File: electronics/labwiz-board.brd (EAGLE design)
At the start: 98.8 x 51 mm, 100 parts, among them J1 SD_MICRO_SDIO_1BIT, J2 CORTEX_DEBUGSMD_original, J3 DNP, U1 STM32F10XRXT6, U2 MCP73831/2, U4 MIC5219-3.3V, X2 M12_BOTTOM_CONTACTS_FPC_1MM, Y3 32.768kHz

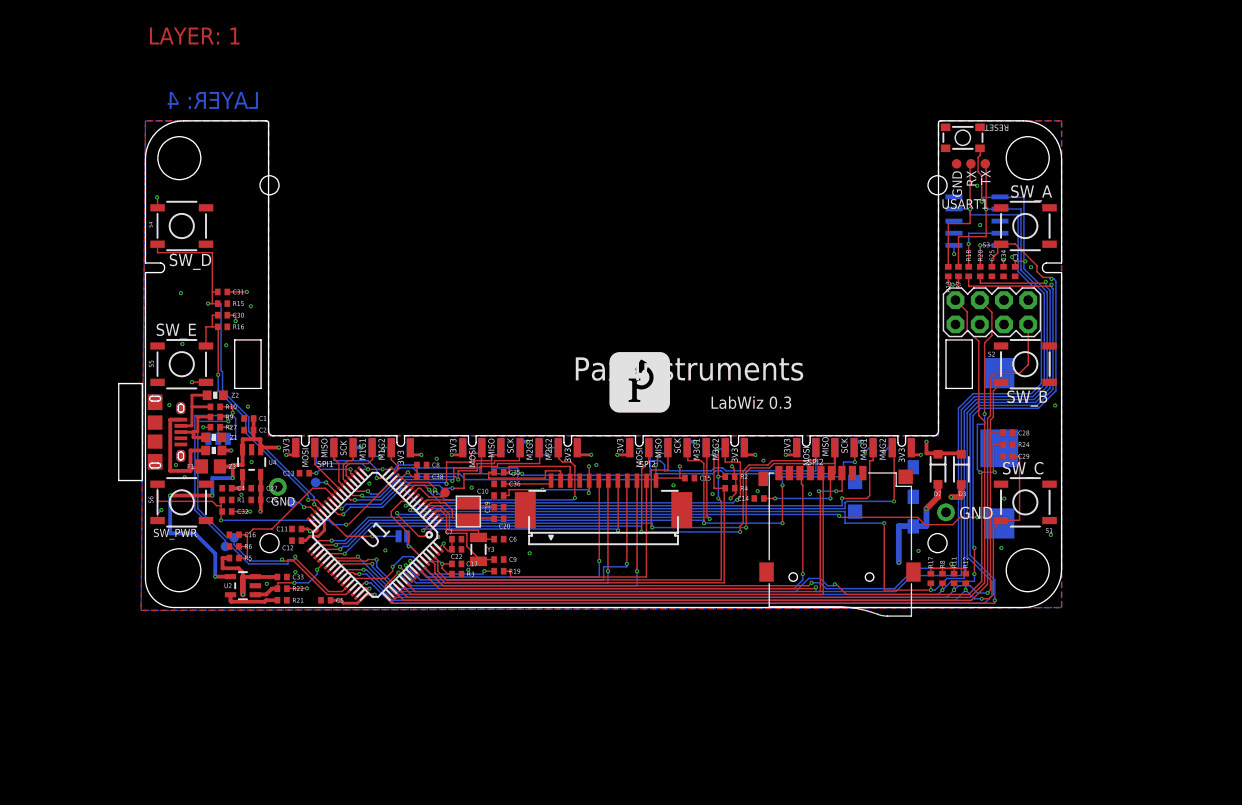
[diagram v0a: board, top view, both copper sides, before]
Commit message: Changed board top edge; extended 24 mil, created protrusion to lock in with top panel of enclosure. Closes #97.
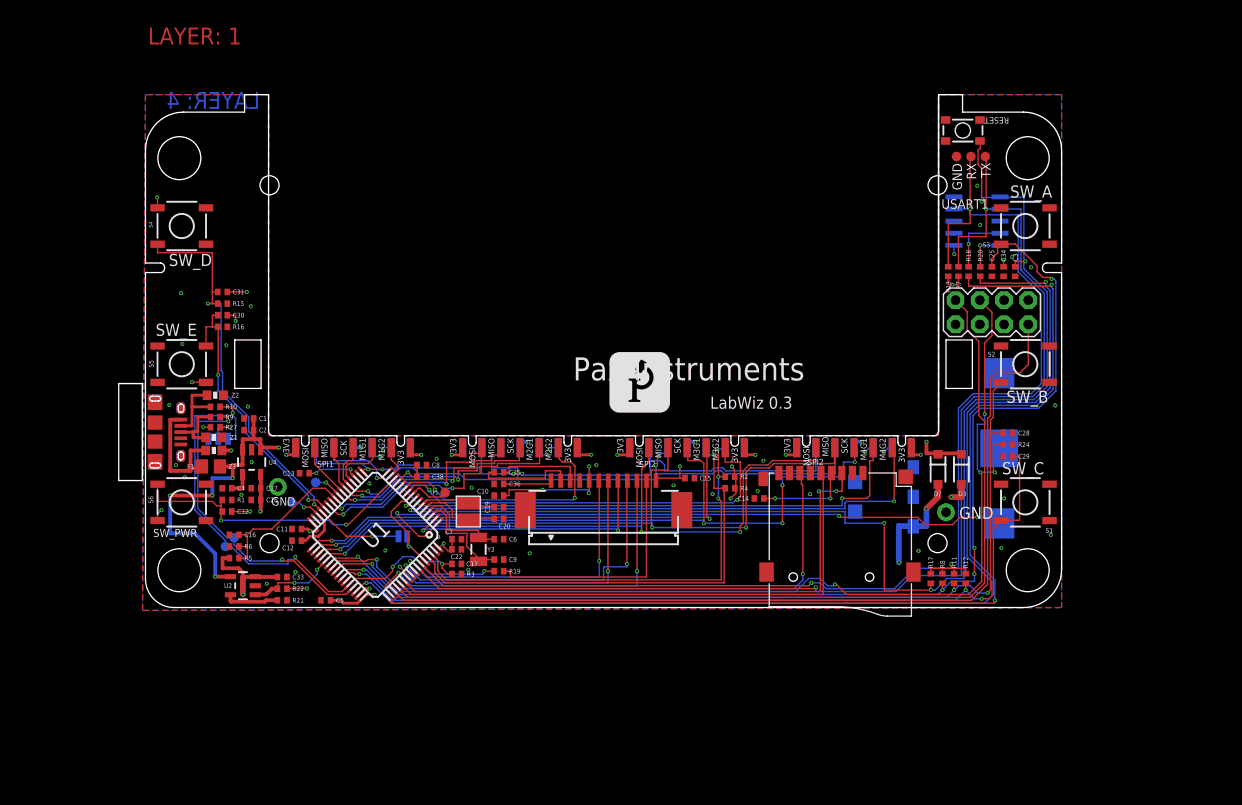
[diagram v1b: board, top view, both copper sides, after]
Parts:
- moved S7 0.76 mm to (85.6, 50.0)
- moved TP10 0.76 mm to (85.0, 47.3)
- moved TP8 0.76 mm to (88.0, 47.3)
- moved TP9 0.76 mm to (86.5, 47.3)
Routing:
- net USART1_TX: track 122.9 -> 123.7 mm
- net USART1_RX: track 124.6 -> 125.4 mm
- net NRST: track 129.7 -> 130.4 mm
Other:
- board size 98.8 x 51 mm -> 98.8 x 53.7 mm

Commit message: Added 2x2 right angle header to board. Closes #105.
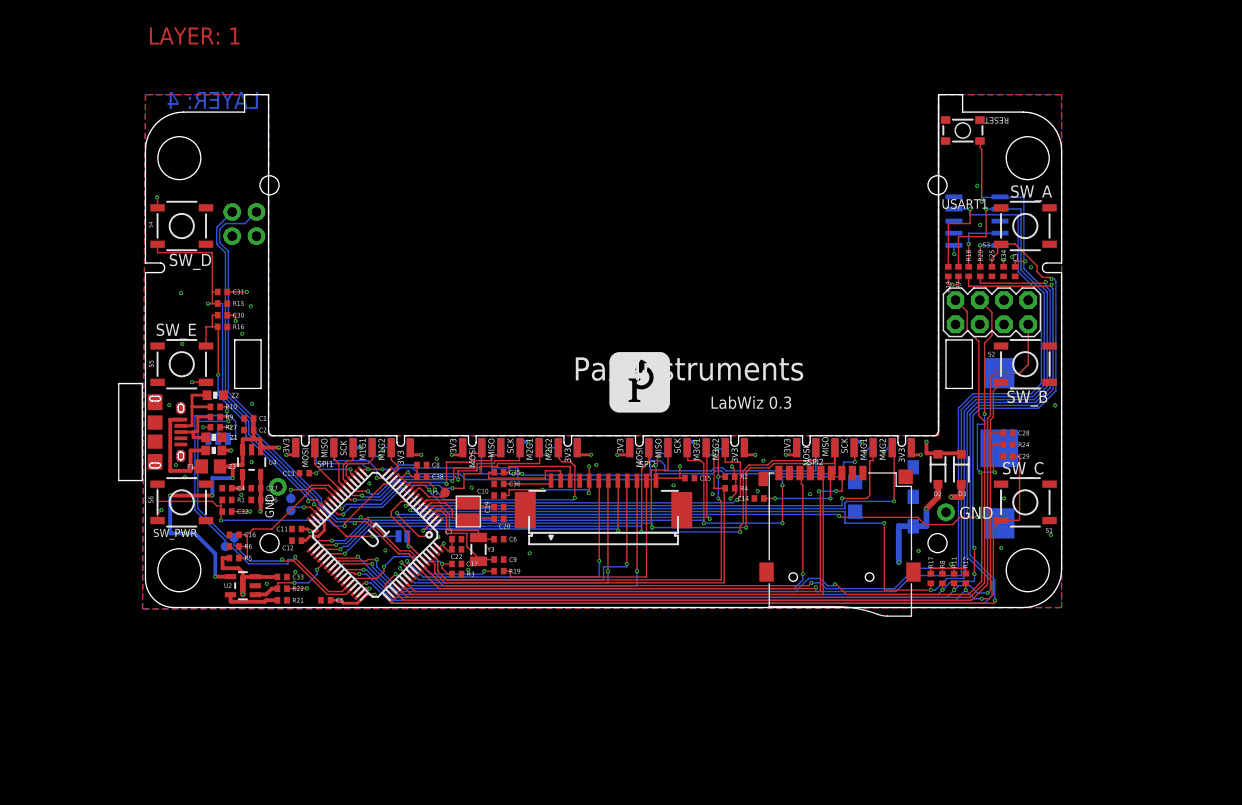
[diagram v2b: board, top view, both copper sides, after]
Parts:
- removed TP10, TP8, TP9: DNP, PaxInstruments-Connectors:PAD_1MM
- added U$5: USART1, PaxInstruments-Connectors:M02X2_TH_RIGHT_ANGLE
- moved TP2 3.09 mm to (15.2, 11.4)
- moved TP7 0.86 mm to (15.2, 10.2)
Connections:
- net GND: now also U$5.4; no longer TP10.P$1
- net USART1_RX: now also U$5.3; no longer TP9.P$1
- net USART1_TX: now also U$5.1; no longer TP8.P$1
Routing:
- net USART1_RX: track 125.4 -> 171.0 mm, vias 2 -> 3
- net USART1_TX: track 123.7 -> 167.6 mm, vias 2 -> 3
- net PC4: track 2.92 -> 6.48 mm
- net LCD_RST: track 35.5 -> 36.6 mm
- net USB_DM: track 40.9 -> 40.1 mm

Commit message: Moved to ESP-09 WiFi modules. Still some work to be done.
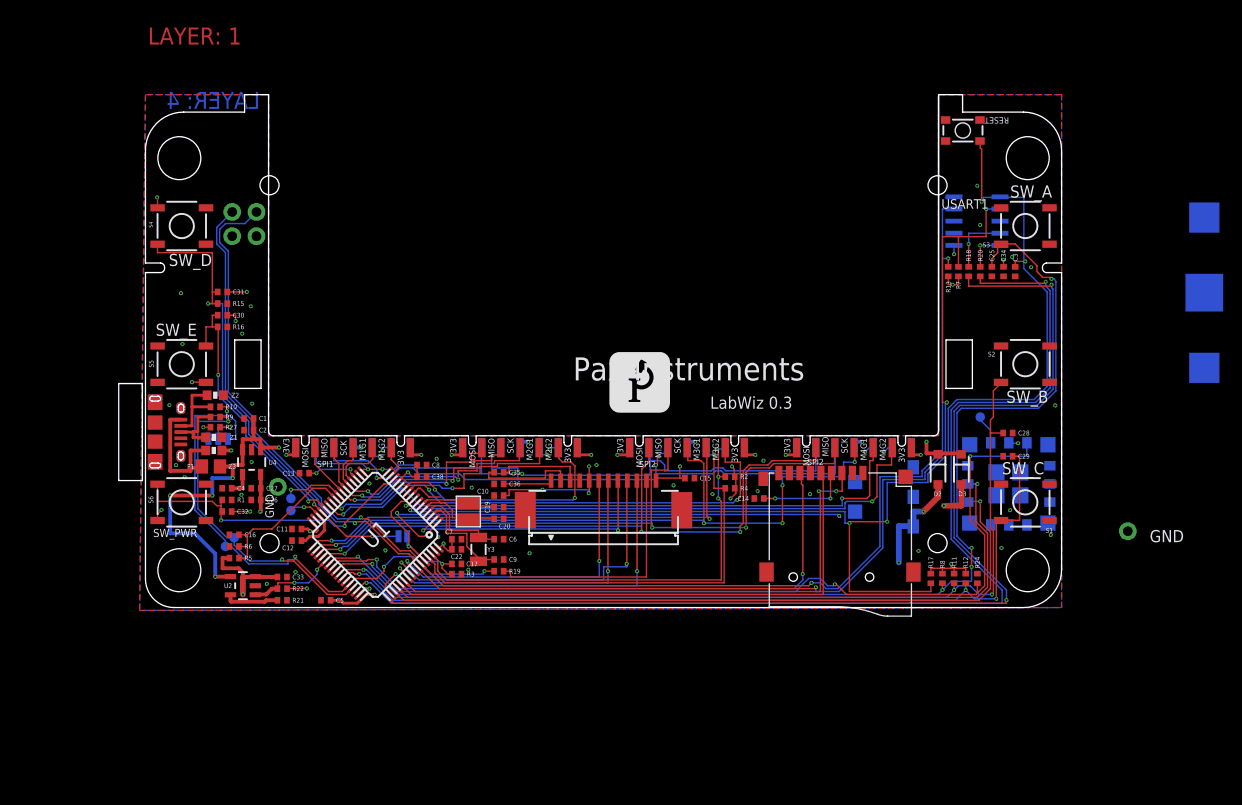
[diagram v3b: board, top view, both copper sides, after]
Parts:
- removed J3: DNP, SparkFun-Connectors:2X4
- added U$7: ESP09, PaxInstruments-DigitalIC:ESP09
- moved TP1 56.6 mm to (87.5, 20.0), flipped to the bottom
- moved BAT1 27.0 mm to (111.0, 33.0)
- moved TP3 19.2 mm to (102.9, 8.00)
- moved R24 14.4 mm to (87.2, 3.05), turned to 90 degrees
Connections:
- new net N$13: TP1.P$1, U$7.ANT
- net 3.3V: now also U$7.VCC; no longer J3.8
- net GND: now also U$7.GND, U$7.GND1, U$7.GND2, U$7.GND3, U$7.GND4, U$7.GND5, U$7.GND6, U$7.GND7; no longer J3.1
- net PC1_BOOT0: no longer TP1.P$1
- net USART3_RX: now also U$7.TX; no longer J3.2
- net USART3_TX: now also U$7.RX; no longer J3.7
- net WIFI_EN: now also U$7.CH_PD; no longer J3.4
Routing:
- net USART1_RX: track 171.0 -> 145.6 mm
- net USART3_TX: track 93.6 -> 74.2 mm, vias 0 -> 1
- net USART3_RX: track 93.3 -> 75.0 mm, vias 0 -> 1
- net RTC_BAT: track 70.7 -> 52.8 mm, vias 3 -> 2
- net USART1_TX: track 167.6 -> 151.9 mm, vias 3 -> 4
- net WIFI_EN: track 108.4 -> 95.2 mm, vias 5 -> 3
- net SWDIO: track 117.3 -> 121.8 mm
- net SWCLK: track 115.2 -> 119.5 mm
- net N$13: track 0.00 -> 3.16 mm
- net 3.3V: track 97.2 -> 99.8 mm, vias 36 -> 37
- net SW_A: track 120.8 -> 123.1 mm
- net NRST: track 130.2 -> 131.6 mm
- net SW_B: track 95.2 -> 95.9 mm
- net MOD4_GPIO2: track 59.1 -> 58.4 mm
- net PC1_BOOT0: track 22.2 -> 21.6 mm

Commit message: Added pin interrupt info to a page on the pin-map spreadsheet. Changed RTC battery to a CR1025. CR1025 connections still need to be routed.
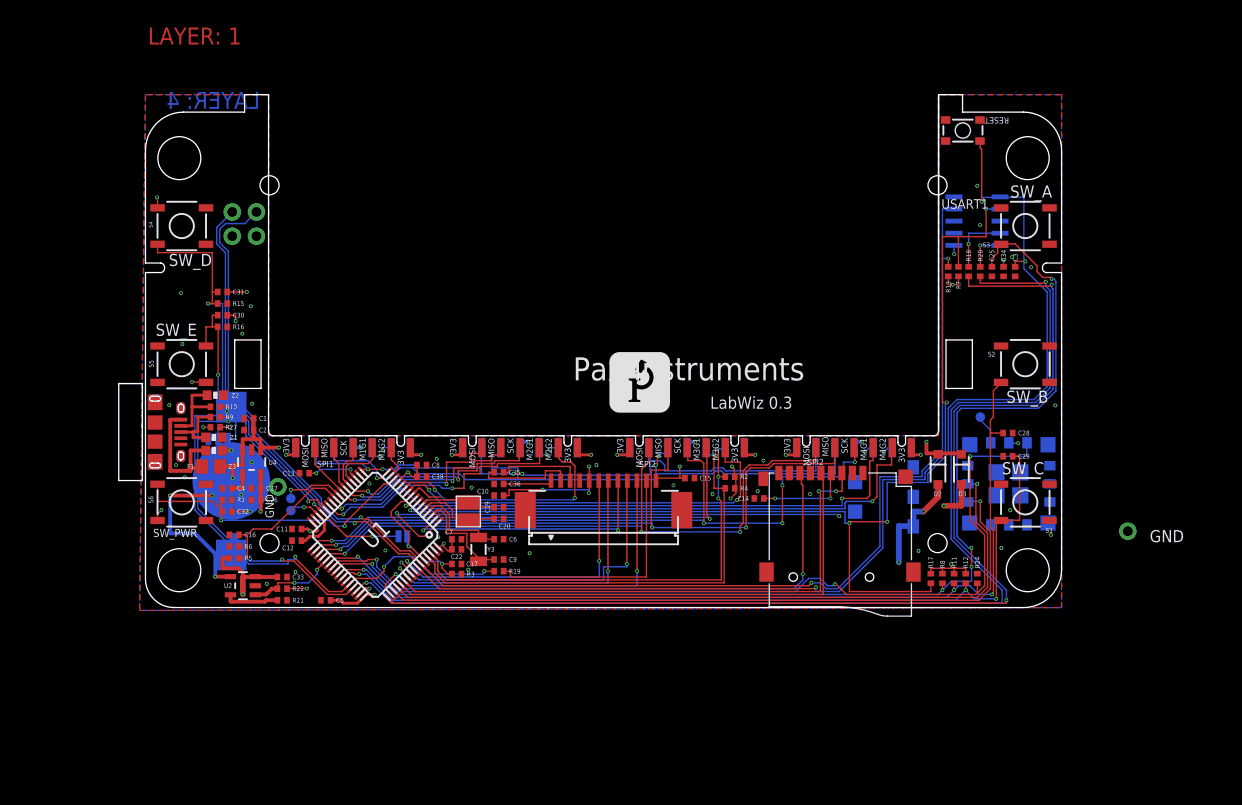
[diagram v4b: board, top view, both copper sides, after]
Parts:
- removed BAT1: (no value), PaxInstruments-Electromechanical:BATTCON_12MM
- added U$8: CR1025, PaxInstruments-Electromechanical:CR2025
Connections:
- net GND: now also U$8.P$1; no longer BAT1.GND
- net RTC_BAT: now also U$8.P$2, U$8.P$3; no longer BAT1.PWR@1
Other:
- board text added: "10 mm CR1025"
- board text added: "12.5 mm CR1220 in T400"

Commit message: Routed the RTC battery. Bumped a bunch of traces around.
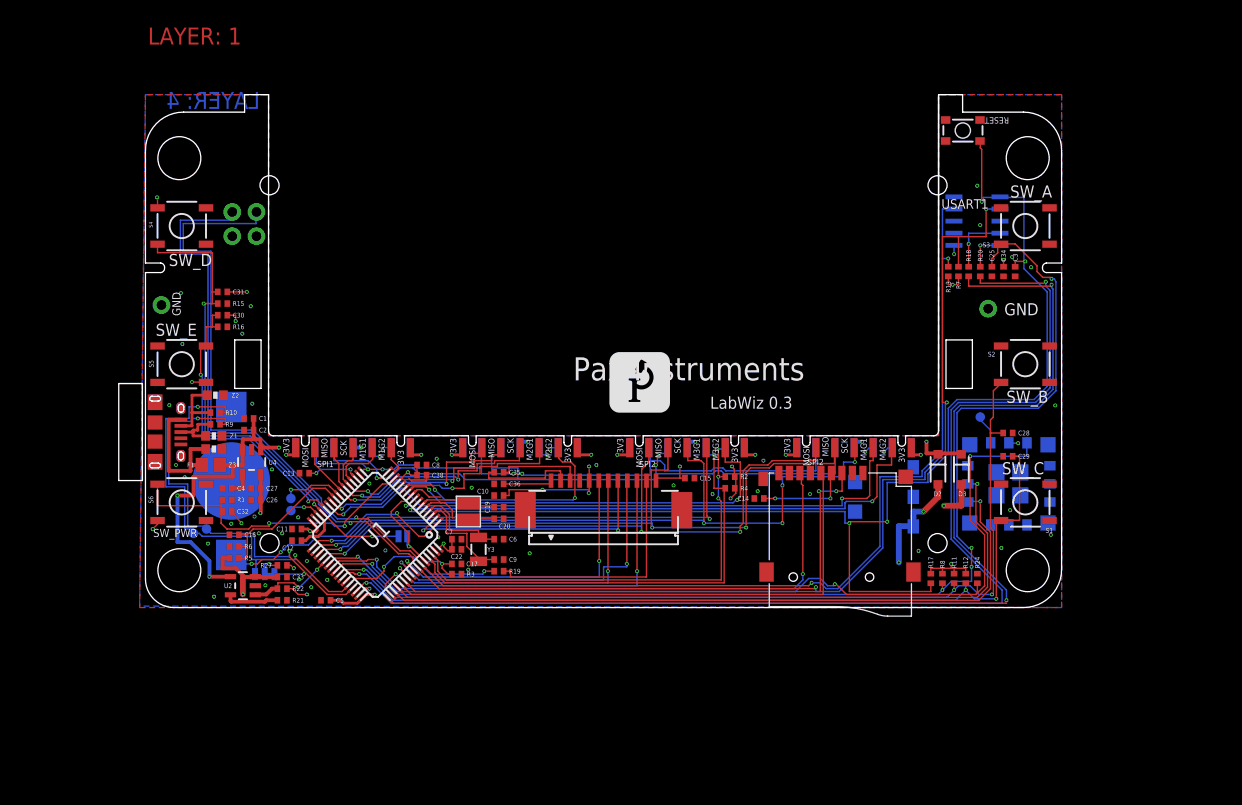
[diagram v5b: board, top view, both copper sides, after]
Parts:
- moved TP3 27.5 mm to (88.3, 31.3)
- moved TP4 22.6 mm to (1.68, 31.7)
- moved R27 16.1 mm to (14.3, 4.42), turned to 0 degrees
- moved JP2 15.0 mm to (12.5, 3.51), turned to 180 degrees
- moved TP6 3.62 mm to (5.03, 7.77)
- moved TP5 3.04 mm to (6.40, 8.23)
- moved R9 0.76 mm to (7.32, 19.2)
- moved R10 0.61 mm to (7.32, 20.4)
- moved C38 0.15 mm to (29.0, 13.9)
- moved F1 0.15 mm to (6.86, 14.9)
- moved Z1 0.15 mm to (7.16, 18.0)
- moved Z3 0.15 mm to (7.16, 16.6)
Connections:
- new net +: U$8.P$2
- net RTC_BAT: no longer U$8.P$2
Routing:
- net RTC_BAT: track 52.8 -> 26.3 mm, vias 2 -> 3
- net USB_DP: track 36.5 -> 48.0 mm, vias 2 -> 3
- net USART1_TX: track 151.9 -> 162.7 mm
- net USART1_RX: track 145.6 -> 156.4 mm
- net USB_DM: track 40.1 -> 46.6 mm
- net SW_D_BOOT0: track 50.3 -> 52.9 mm
- net SW_E_BOOT1: track 29.4 -> 31.6 mm
- net GND: track 2.40 -> 4.01 mm, vias 36 -> 44
- net VBUS: track 123.2 -> 121.8 mm, vias 10 -> 8
- net SW_PWR: track 31.7 -> 32.9 mm
- net N$5: track 3.46 -> 2.55 mm
- net D+: track 6.57 -> 5.65 mm
- net USB_VCC: track 13.7 -> 14.3 mm
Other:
- board text removed: "10 mm CR1025"
- board text removed: "12.5 mm CR1220 in T400"

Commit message: PC4 is now VBUS_DETECT. Removed unnecessary USB data series resistors. Closes #76.'
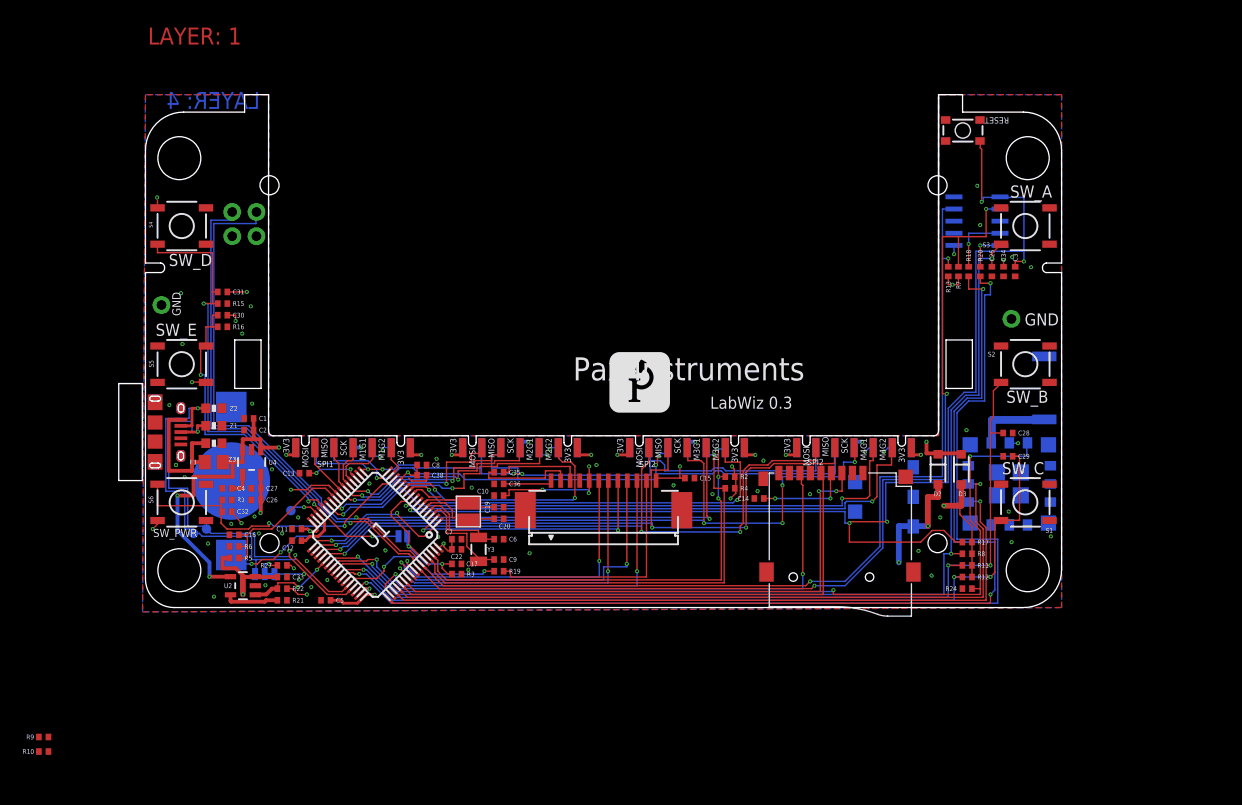
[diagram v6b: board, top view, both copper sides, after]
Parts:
- removed TP1, TP2: DNP, PaxInstruments-Connectors:PAD_1MM
- added U$10: 2.45GHz, SparkFun-RF:ANT-2.4GHZ-6.5X2.2MM
- R10: value 22R -> 47k
- R9: value 22R -> 68k
- moved R10 39.8 mm to (-10.7, -15.1)
- moved R9 37.4 mm to (-10.7, -13.6)
- moved R17 5.39 mm to (86.1, 6.86), turned to 180 degrees
- moved R8 3.66 mm to (86.1, 5.64), turned to 180 degrees
- moved TP3 2.66 mm to (90.7, 30.2)
- moved R11 1.94 mm to (86.1, 4.42), turned to 180 degrees
- moved R24 1.51 mm to (86.1, 1.98), turned to 180 degrees
- moved Z2 1.38 mm to (7.16, 20.9)
- moved Z1 1.07 mm to (7.16, 19.1)
- moved Z3 0.61 mm to (7.16, 17.2)
- moved F1 0.43 mm to (7.16, 15.2)
- moved R12 0.22 mm to (86.1, 3.20), turned to 180 degrees
- moved U$7 0.05 mm to (90.5, 13.0)
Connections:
- removed net D+: R9.1, U$1.PIN$3, Z1.2
- removed net D-: R10.1, U$1.PIN$2, Z2.2
- removed net PC4: TP2.P$1, U1.24
- new net VBUS_DETECT: R10.2, R9.1, U1.24
- net GND: now also R9.2
- net N$13: now also U$10.FEED; no longer TP1.P$1
- net USB_DM: now also U$1.PIN$2, Z2.2; no longer R10.2
- net USB_DP: now also U$1.PIN$3, Z1.2; no longer R9.2
- net VBUS: now also R10.1
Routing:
- net SWCLK: track 119.5 -> 105.8 mm
- net SW_A: track 123.1 -> 109.8 mm, vias 5 -> 3
- net SWDIO: track 121.8 -> 111.0 mm
- net D-: track 7.91 -> 0.00 mm
- net PC4: track 6.48 -> 0.00 mm, vias 1 -> 0
- net USART1_TX: track 162.7 -> 156.6 mm
- net USART1_RX: track 156.4 -> 150.4 mm
- net D+: track 5.65 -> 0.00 mm
- net VBUS_DETECT: track 0.00 -> 5.56 mm, vias 0 -> 1
- net N$13: track 3.16 -> 7.94 mm
- net NRST: track 131.6 -> 129.0 mm
- net 3.3V: track 99.6 -> 101.2 mm, vias 37 -> 36
- net VBUS: track 121.8 -> 120.7 mm
- net WIFI_EN: track 95.2 -> 94.2 mm
- net VBAT: track 95.0 -> 95.8 mm
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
